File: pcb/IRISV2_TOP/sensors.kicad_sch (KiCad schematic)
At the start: 22 parts, among them U5 MMC5983MA, U6 ICM-45686, U7 ICM-45686, U8 BMP581

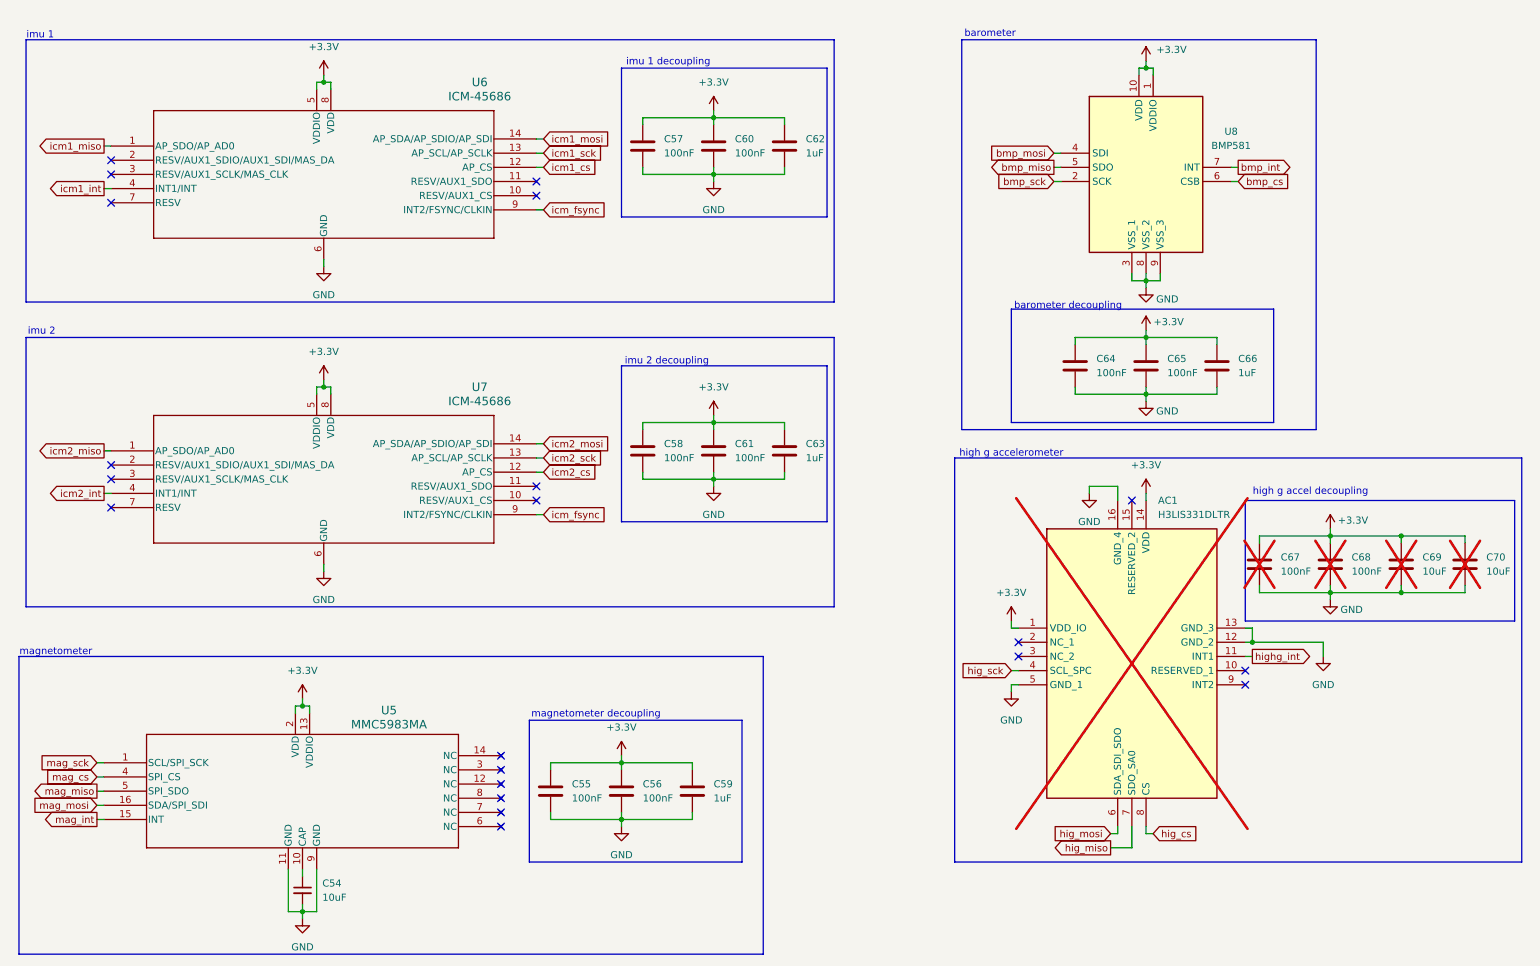
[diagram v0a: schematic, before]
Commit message: split into subprojects, fixed up stuff, started real pcb work
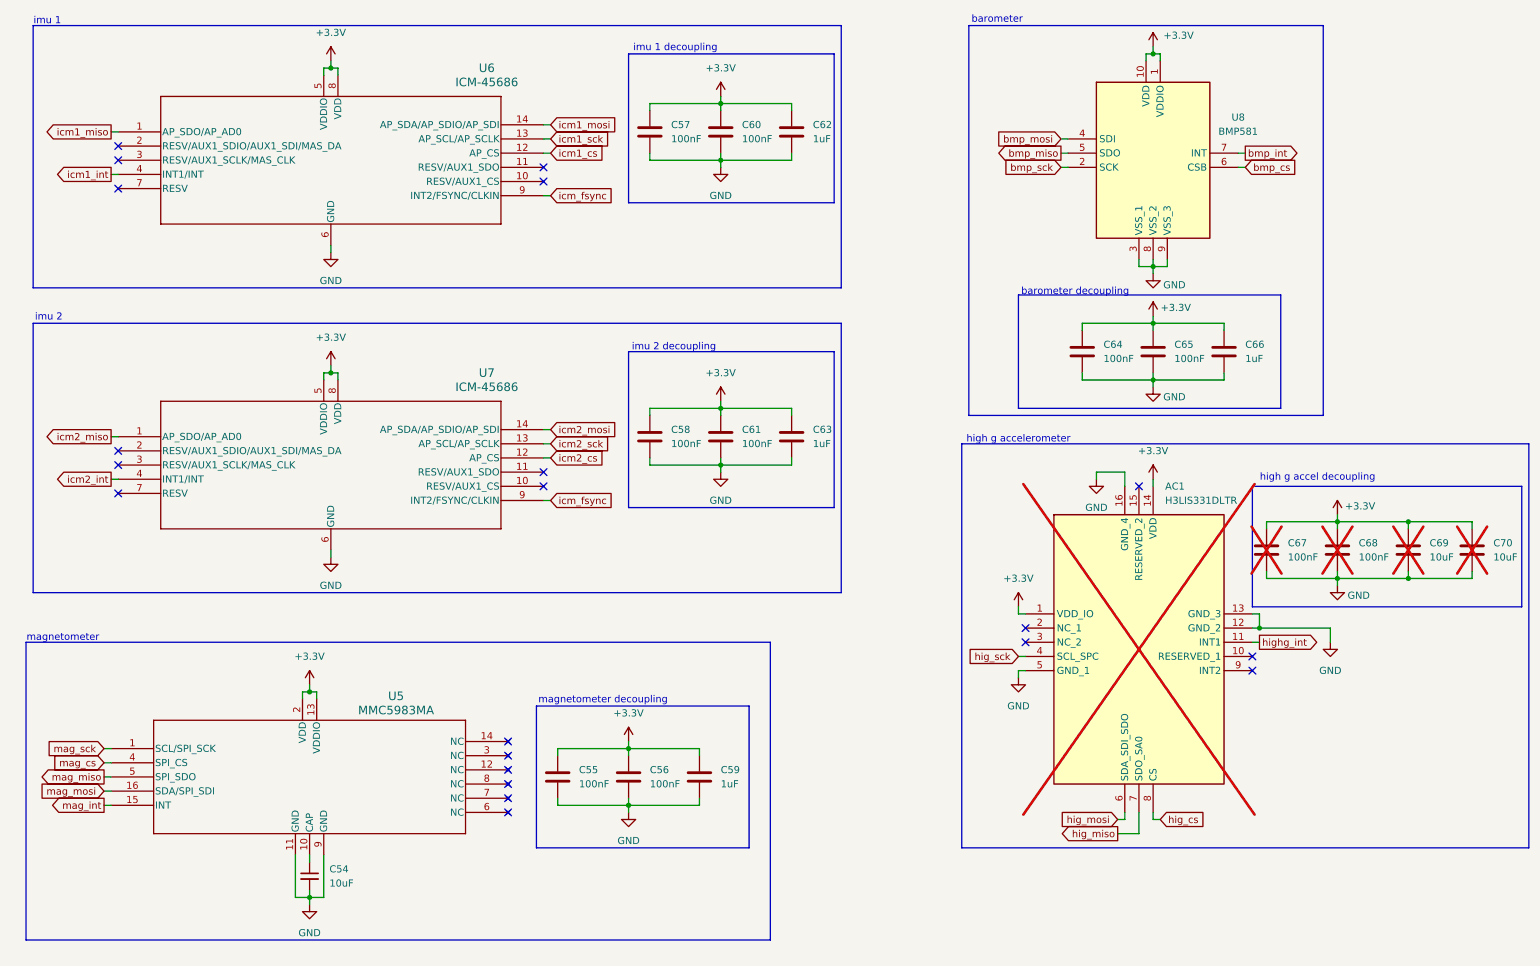
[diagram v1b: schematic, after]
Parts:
- U5: footprint mmc5983ma:MMC5983MA_MEM -> MMC5983MA:MMC5983MA_MEM
- U6, U7: footprint icm45686:U_2p5X3X0p81_LGA14L_TDK -> ICM-45686:U_2p5X3X0p81_LGA14L_TDK
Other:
- moved on the sheet: AC1, C54, C55, C56, C57, C58, C59, C60, C61, C62, C63, C64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

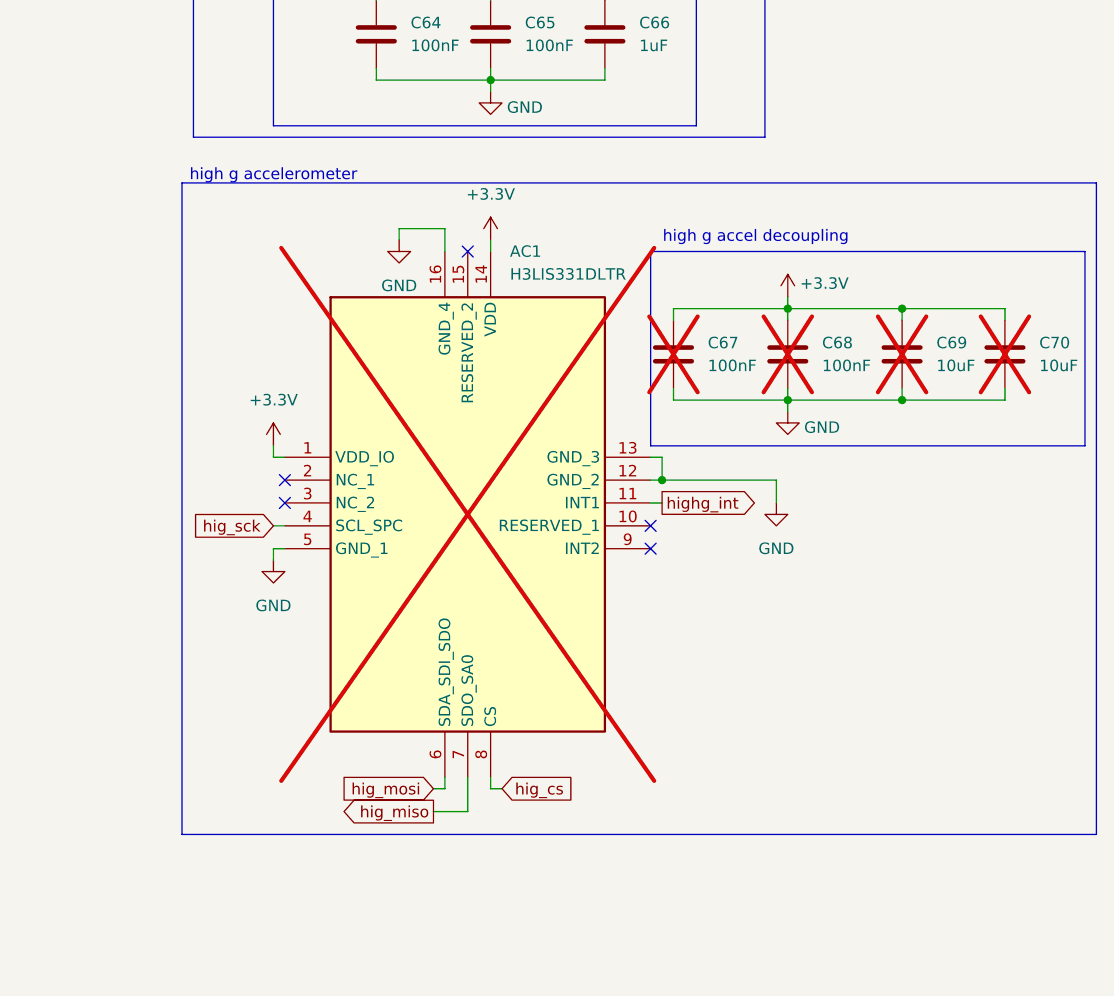
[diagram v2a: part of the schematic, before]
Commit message: removed high g accel, top board layout looking decent, routing started also - though i realized i was missing the micro sd card and that's going to be a pain to add
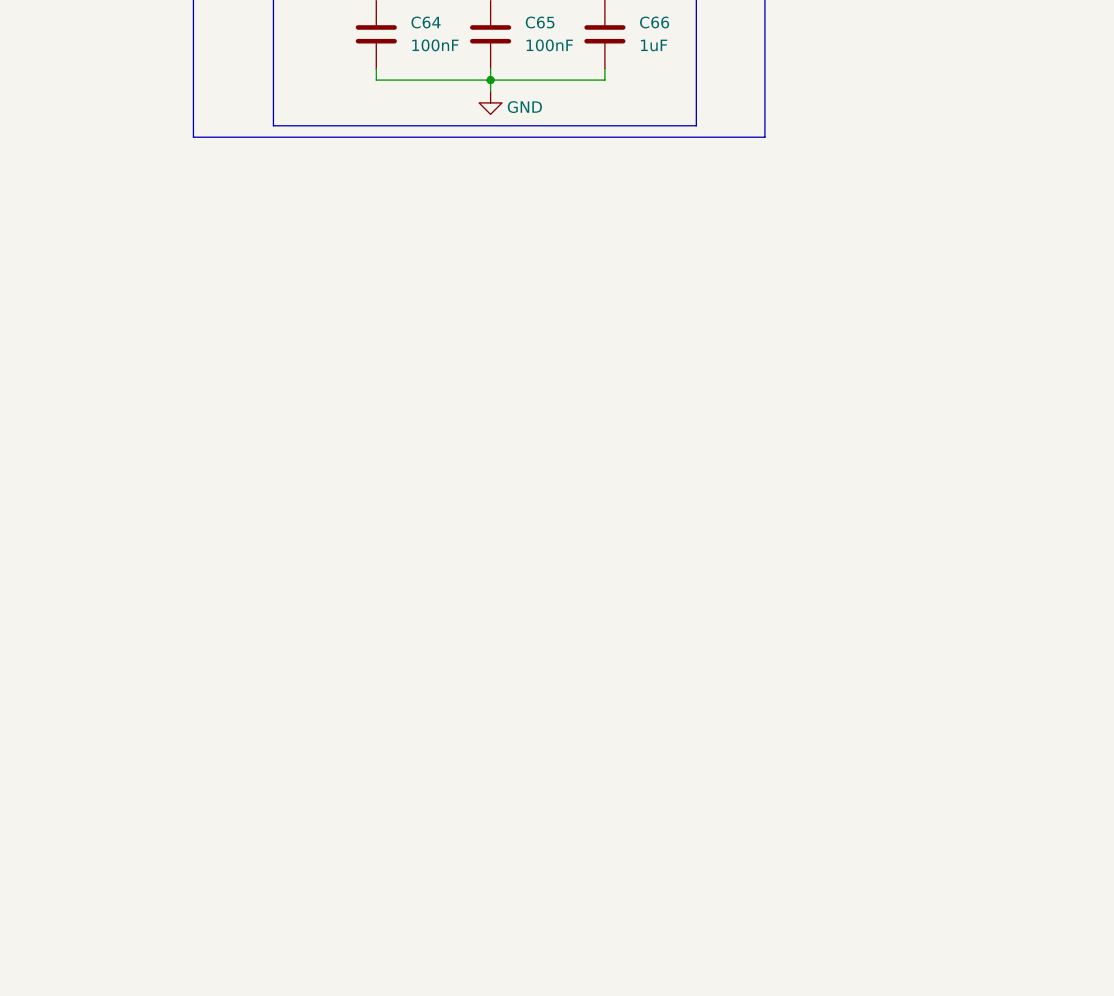
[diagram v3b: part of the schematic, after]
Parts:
- removed AC1: H3LIS331DLTR, H3LIS331DLTR:LIS3DHTR, symbol H3LIS331DLTR:H3LIS331DLTR
- removed C67, C68: 100nF, Capacitor_SMD:C_0402_1005Metric, symbol Device:C
- removed C69, C70: 10uF, Capacitor_SMD:C_0603_1608Metric, symbol Device:C
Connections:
- no-connect marks 21 -> 16
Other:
- note removed: "high g accel decoupling"
- note removed: "high g accelerometer"
